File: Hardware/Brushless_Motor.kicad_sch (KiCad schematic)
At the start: 0 parts

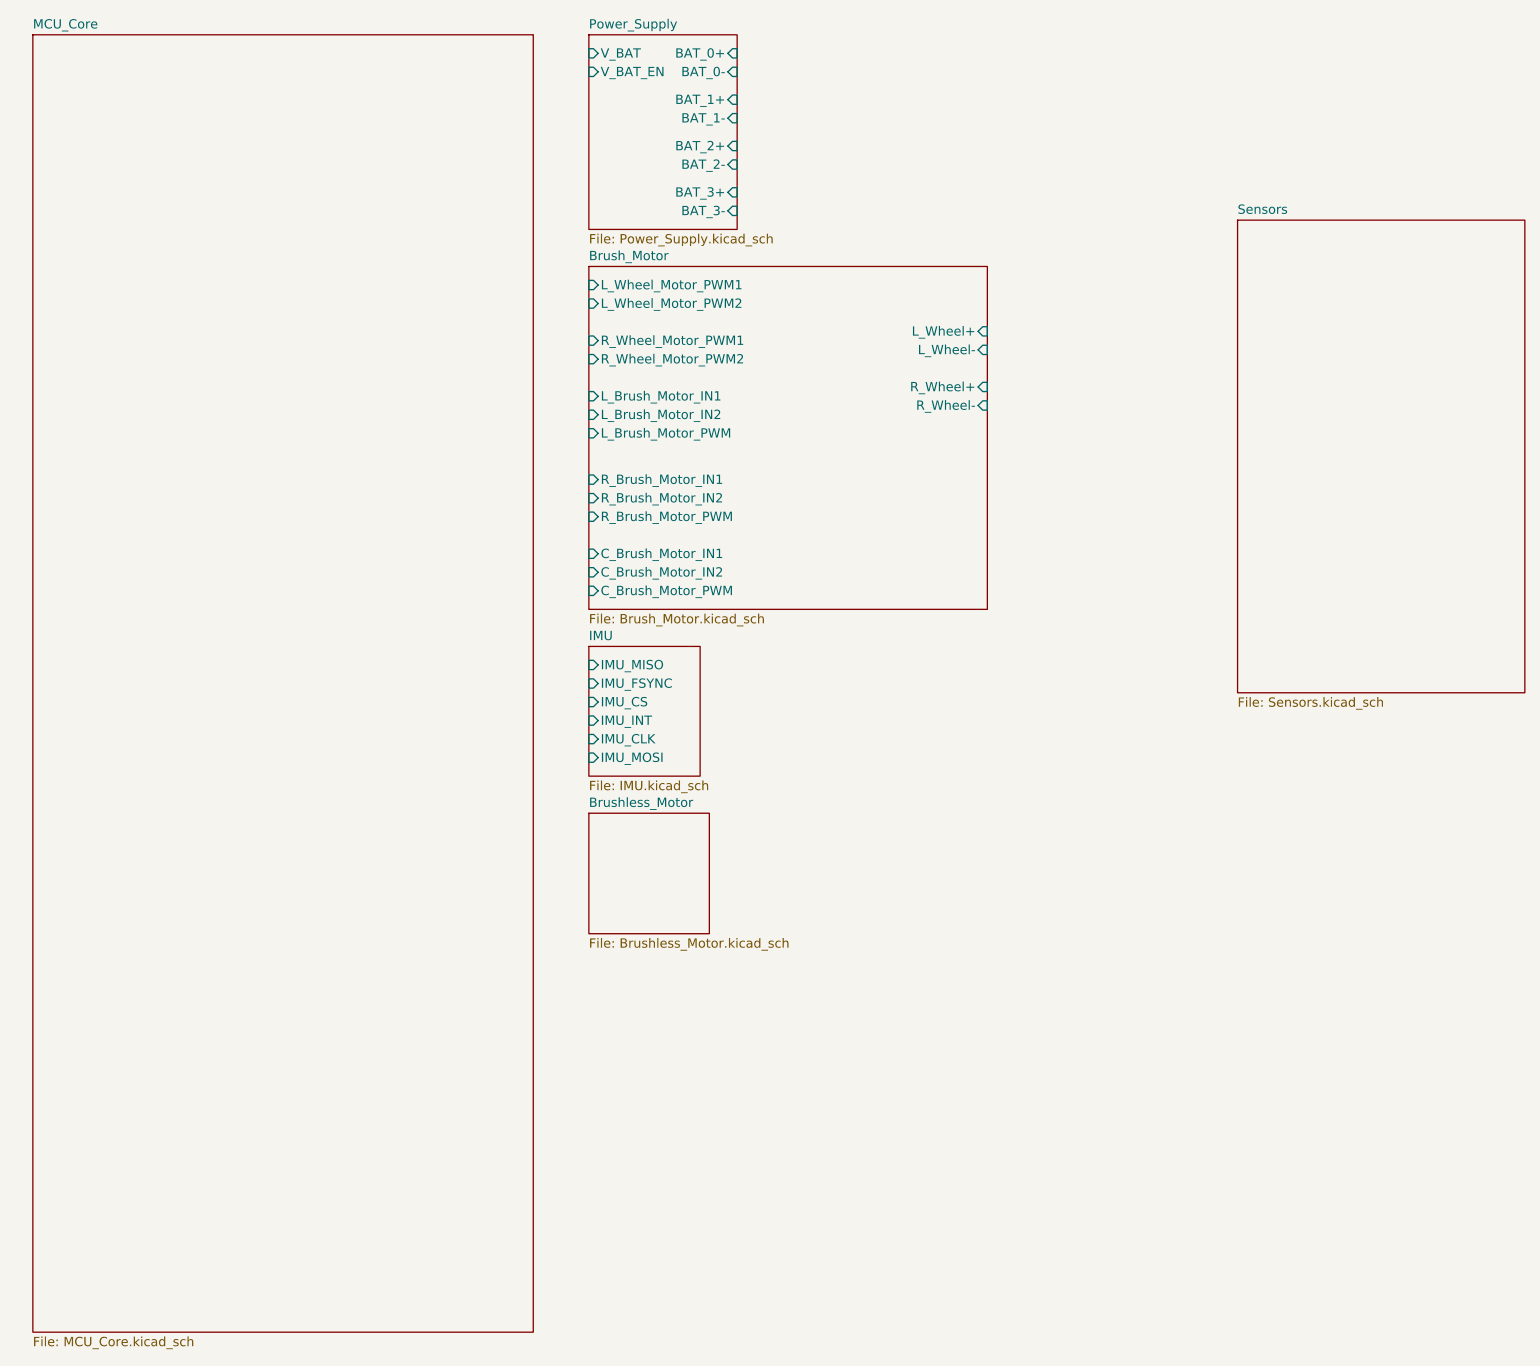
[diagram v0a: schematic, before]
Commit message: Add Image Transmission
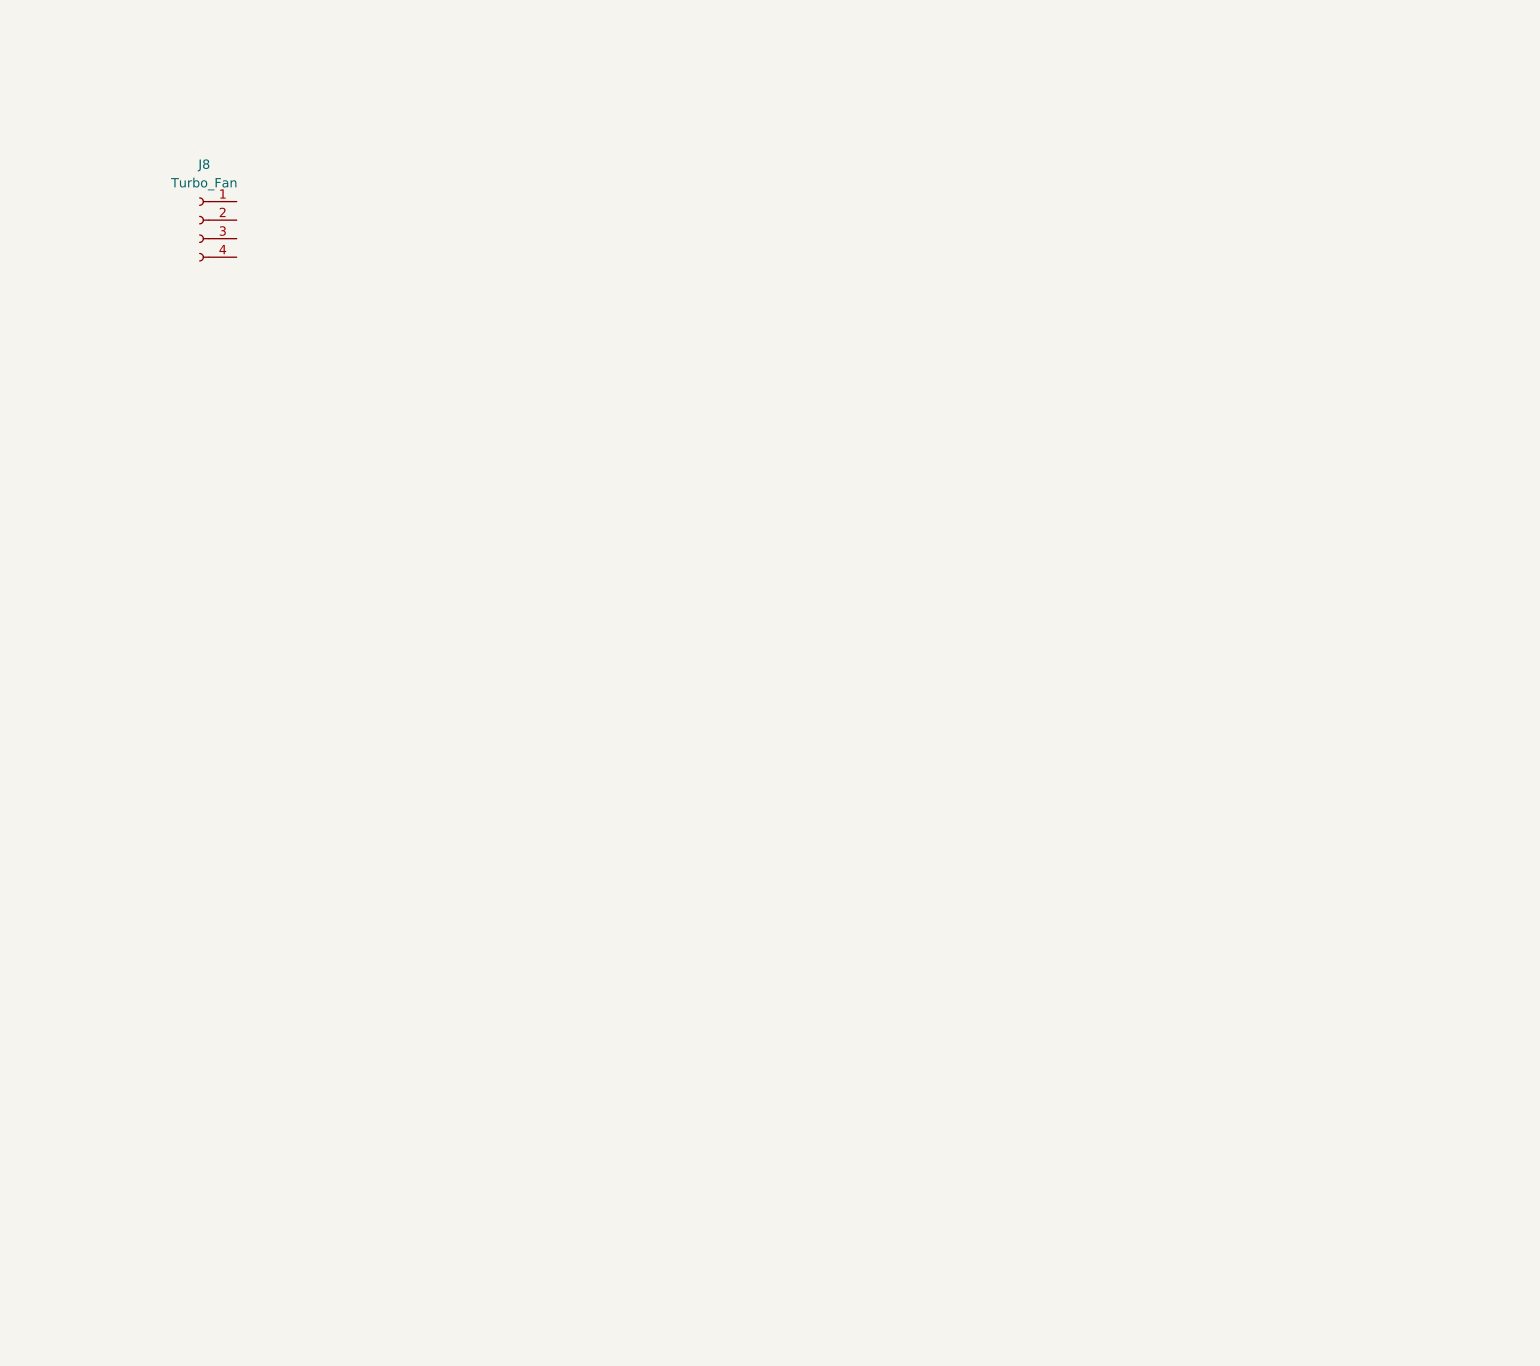
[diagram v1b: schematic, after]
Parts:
- added J8: Turbo_Fan, symbol Connector:Conn_01x04_Socket
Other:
- removed sheet Brush_Motor
- removed sheet Brushless_Motor
- removed sheet IMU
- removed sheet MCU_Core
- removed sheet Power_Supply
- removed sheet Sensors

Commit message: Update PCB
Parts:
- removed J8: Turbo_Fan, symbol Connector:Conn_01x04_Socket
- added C72, C73, C74, C75: 0.1uF, Capacitor_SMD:C_0603_1608Metric, symbol Library:C
- added R62, R63, R64, R65: 1K, Resistor_SMD:R_0603_1608Metric, symbol Library:R
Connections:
- new net: C72.2, R62.2, R63.1
- new net: C74.2, R64.2, R65.1
- new net GND: C72.1, C73.1, C74.1, C75.1, R62.1, R64.1
- new net Turbo_FB_OUT: C75.2, R65.2
- new net Turbo_PWM_OUT: C73.2, R63.2
